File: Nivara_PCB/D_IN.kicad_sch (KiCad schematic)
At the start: 0 parts

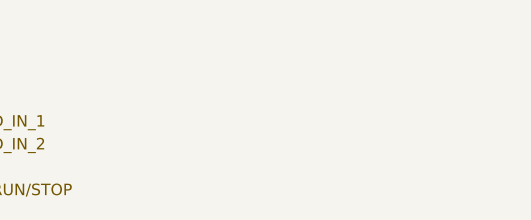
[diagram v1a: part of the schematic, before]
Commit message: Añadido de funciones NPN/PNP
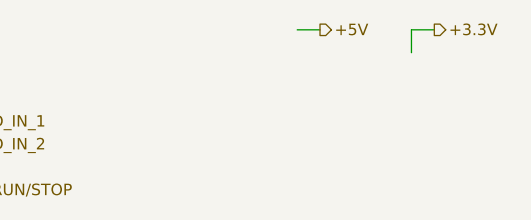
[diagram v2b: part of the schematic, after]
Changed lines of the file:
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@@
 	(generator_version "9.0")
 	(paper "A4")
+	(wire
+		(pts
+			(xy 107.95 71.12) (xy 107.95 73.66)
+		)
+		(stroke
+			(width 0)
+			(type default)
+		)
+	)
+	(wire
+		(pts
+			(xy 95.25 71.12) (xy 97.79 71.12)
+		)
+		(stroke
+			(width 0)
+			(type default)
+		)
+	)
+	(wire
+		(pts
+			(xy 110.49 71.12) (xy 107.95 71.12)
+		)
+		(stroke
+			(width 0)
+			(type default)
+		)
+	)
 	(hierarchical_label "D_IN_2"
 		(shape input)
 		(at 59.69 83.82 0)
+		(effects
+			(font
+				(size 1.27 1.27)
+			)
+			(justify left)
+		)
+	)
+	(hierarchical_label "+5V"
+		(shape output)
+		(at 97.79 71.12 0)
 		(effects
 			(font
@@
 		(effects
 			(font
+				(size 1.27 1.27)
+			)
+			(justify left)
+		)
+	)
+	(hierarchical_label "+3.3V"
+		(shape output)
+		(at 110.49 71.12 0)
+		(effects
+			(font

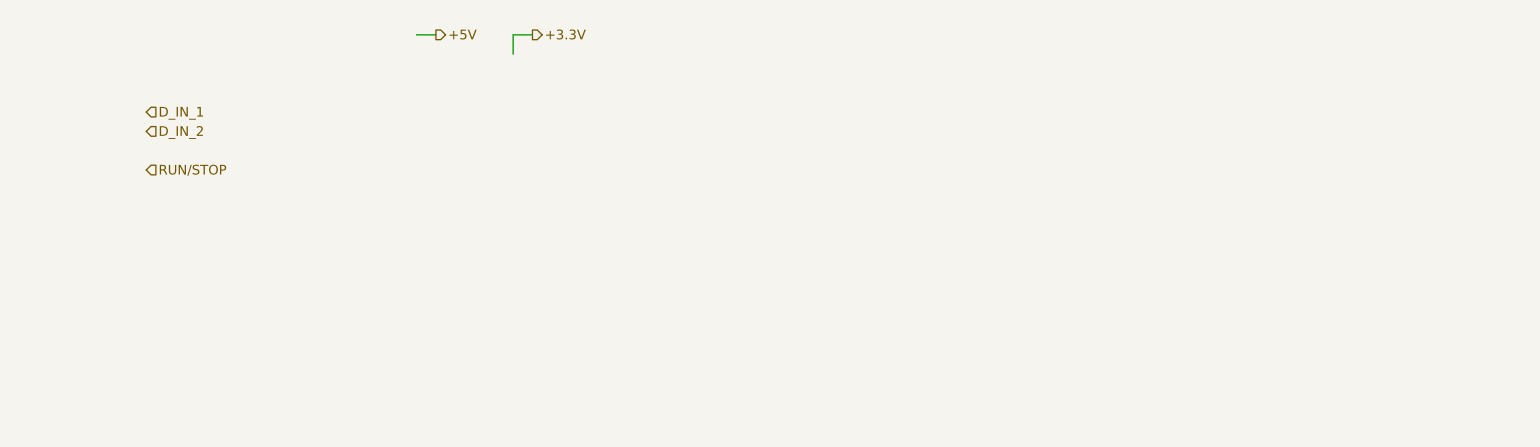
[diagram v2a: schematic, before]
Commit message: Cambios en las mediciones análogas.
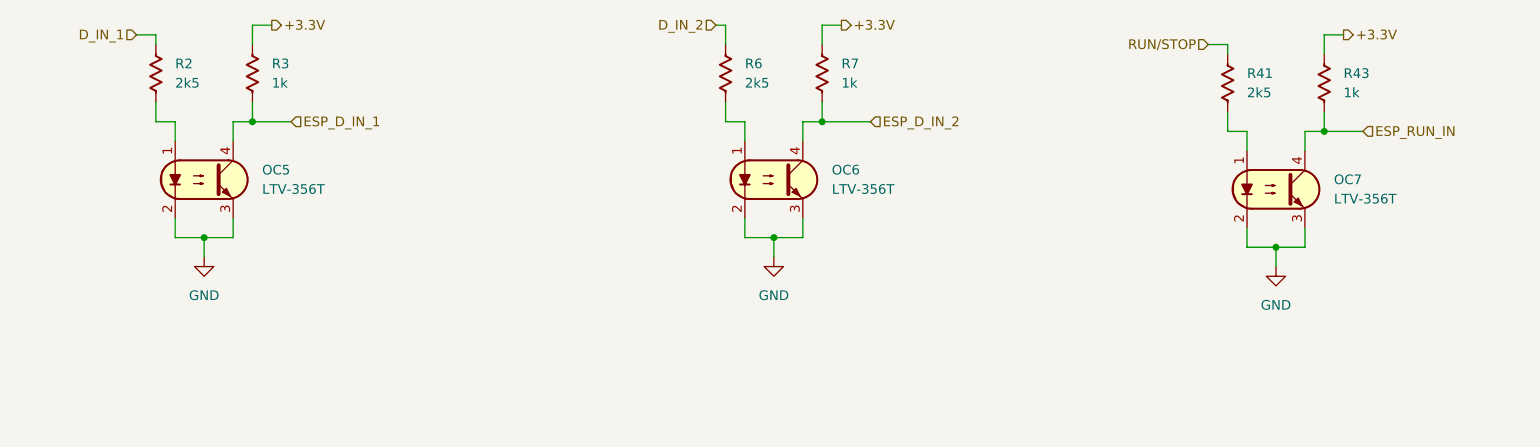
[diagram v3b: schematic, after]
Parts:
- added OC5, OC6, OC7: LTV-356T, PCM_Package_SO_AKL:SO-4_4.4x3.9mm_P2.54mm, symbol PCM_Optocoupler_AKL:LTV-356T
- added R2, R41, R6: 2k5, PCM_Resistor_SMD_AKL:R_0603_1608Metric, symbol PCM_Resistor_US_AKL:R_0603
- added R3, R43, R7: 1k, PCM_Resistor_SMD_AKL:R_0603_1608Metric, symbol PCM_Resistor_US_AKL:R_0603
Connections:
- net +3.3V: now also R3.1, R43.1, R7.1
- net D_IN_1: now also R2.1
- net D_IN_2: now also R6.1
- net RUN/STOP: now also R41.1
- new net: OC5.1, R2.2
- new net: OC7.1, R41.2
- new net: OC6.1, R6.2
- new net ESP_D_IN_1: OC5.4, R3.2
- new net ESP_D_IN_2: OC6.4, R7.2
- new net ESP_RUN_IN: OC7.4, R43.2
- new net GND: OC5.2, OC5.3, OC6.2, OC6.3, OC7.2, OC7.3

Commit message: Cambios en las salidas analogicas, ya que el ESP32 S3 no tiene DAC
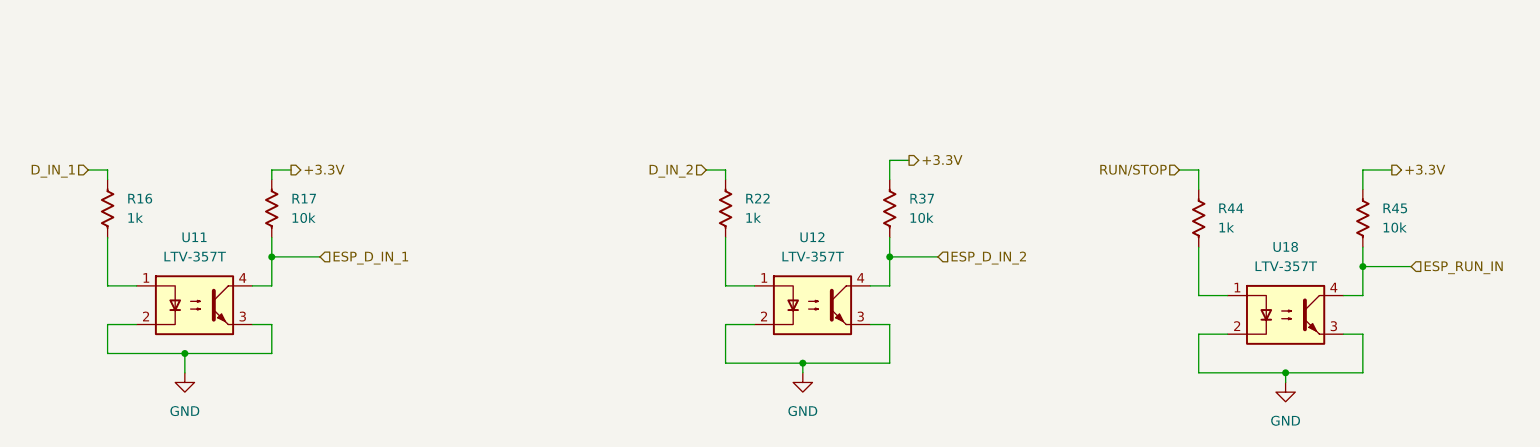
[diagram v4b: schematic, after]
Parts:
- removed OC5, OC6, OC7: LTV-356T, PCM_Package_SO_AKL:SO-4_4.4x3.9mm_P2.54mm, symbol PCM_Optocoupler_AKL:LTV-356T
- removed R2, R41, R6: 2k5, PCM_Resistor_SMD_AKL:R_0603_1608Metric, symbol PCM_Resistor_US_AKL:R_0603
- removed R3, R43, R7: 1k, PCM_Resistor_SMD_AKL:R_0603_1608Metric, symbol PCM_Resistor_US_AKL:R_0603
- added R16, R22, R44: 1k, PCM_Resistor_SMD_AKL:R_0603_1608Metric, symbol PCM_Resistor_US_AKL:R_0603
- added R17, R37, R45: 10k, PCM_Resistor_SMD_AKL:R_0603_1608Metric, symbol PCM_Resistor_US_AKL:R_0603
- added U11, U12, U18: LTV-357T, Package_SO:SO-4_4.4x3.6mm_P2.54mm, symbol Isolator:LTV-357T
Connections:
- net +3.3V: now also R17.1, R37.1, R45.1
- net D_IN_1: now also R16.1
- net D_IN_2: now also R22.1
- net ESP_D_IN_1: now also R17.2, U11.4
- net ESP_D_IN_2: now also R37.2, U12.4
- net ESP_RUN_IN: now also R45.2, U18.4
- net GND: now also U11.2, U11.3, U12.2, U12.3, U18.2, U18.3
- net RUN/STOP: now also R44.1
- new net: R44.2, U18.1
- new net: R22.2, U12.1
- new net: R16.2, U11.1
